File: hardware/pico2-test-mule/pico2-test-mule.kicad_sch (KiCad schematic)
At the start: 70 parts, among them J1 SPEAKER, J2 POWER, J3 AUX, J4 MOTOR, J5 VCC, Q1 DMN2991UDA-7B, Q10 DMN2991UDA-7B, Q11 DMN2991UDA-7B, Q12 DMN2991UDA-7B, Q13 DMN2991UDA-7B, Q2 SS8050, Q3 SS8050, Q4 DMN2991UDA-7B, Q5 SS8050, Q6 SS8050, Q7 NST847BPDP6T5G, Q8 SS8050, Q9 NST847BPDP6T5G, U1 NCS2220AMUT1G, U2 AP63203WU, U3 PICO, U4 MAX98357AEWL+T, U5 MD9927

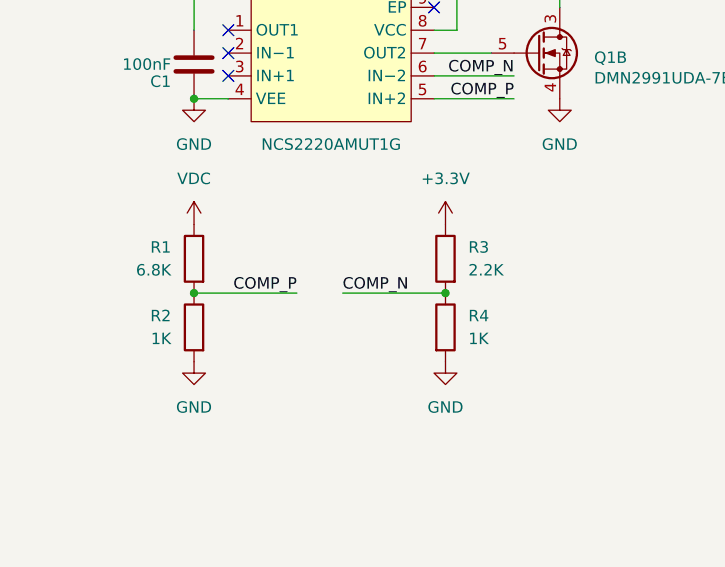
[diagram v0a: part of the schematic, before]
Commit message: fix: un-swap capacitor shutdown circuit inputs
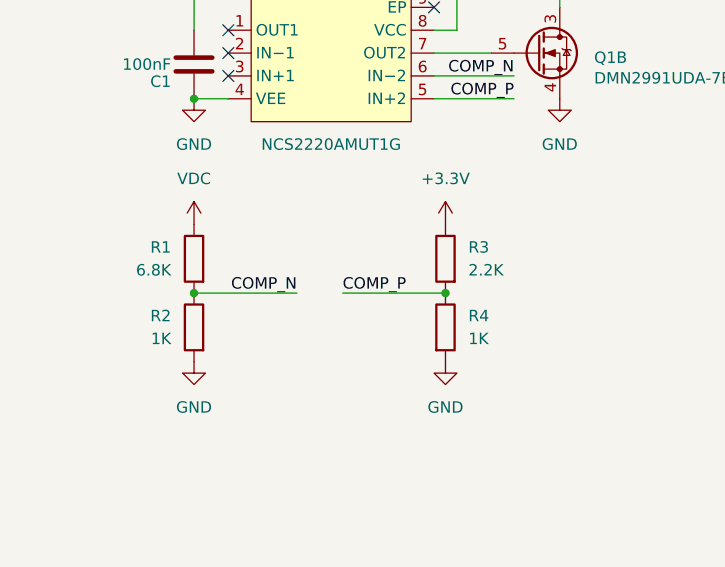
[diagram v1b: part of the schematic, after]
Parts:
- C1, C10, C3, C7, C9: footprint Capacitor_SMD:C_0402_1005Metric -> pico2-test-mule:C_0402_1005Metric
- C2, C4: footprint Capacitor_SMD:C_0603_1608Metric -> pico2-test-mule:C_0603_1608Metric
- C5, C8: footprint Capacitor_SMD:C_1206_3216Metric -> pico2-test-mule:C_1206_3216Metric
- C6: footprint Capacitor_SMD:C_0805_2012Metric -> pico2-test-mule:C_0805_2012Metric
- D10, D11, D12, D14, D15, D16, D17, D19, D3, D4, D5, D6, D9: footprint LED_SMD:LED_0603_1608Metric -> pico2-test-mule:LED_0603_1608Metric
- J1: footprint Connector_PinHeader_2.54mm:PinHeader_1x06_P2.54mm_Vertical -> pico2-test-mule:PinHeader_1x06_P2.54mm_Vertical
- J2: footprint Connector_PinHeader_2.54mm:PinHeader_1x04_P2.54mm_Vertical -> pico2-test-mule:PinHeader_1x04_P2.54mm_Vertical
- J3: footprint Connector_PinHeader_2.54mm:PinHeader_1x05_P2.54mm_Vertical -> pico2-test-mule:PinHeader_1x05_P2.54mm_Vertical
- J4, J5: footprint Connector_PinHeader_2.54mm:PinHeader_1x02_P2.54mm_Vertical -> pico2-test-mule:PinHeader_1x02_P2.54mm_Vertical
- Q2, Q3, Q5, Q6, Q8: footprint Package_TO_SOT_SMD:SOT-23 -> pico2-test-mule:SOT-23
- Q7, Q9: footprint Package_TO_SOT_SMD:SOT-963 -> pico2-test-mule:SOT-963
- R1, R10, R11, R12, R13, R14, R2, R3, R4, R5, R6, R7, R8, R9: footprint Resistor_SMD:R_0402_1005Metric -> pico2-test-mule:R_0402_1005Metric
- RN1, RN2, RN3: footprint Resistor_SMD:R_Array_Concave_4x0402 -> pico2-test-mule:R_Array_Concave_4x0402
- U3: footprint Module:RaspberryPi_Pico_Common_THT -> pico2-test-mule:RaspberryPi_Pico_Common_THT
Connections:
- net COMP_N: now also R1.2, R2.1; no longer R3.2, R4.1
- net COMP_P: now also R3.2, R4.1; no longer R1.2, R2.1
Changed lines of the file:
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@@
 	)
 	(label "COMP_N"
-		(at 58.42 157.48 0)
+		(at 53.34 157.48 180)
 		(effects
 			(font
 				(size 1.27 1.27)
 			)
-			(justify left bottom)
+			(justify right bottom)
 		)
 	)
 	(label "COMP_P"
-		(at 53.34 157.48 180)
+		(at 58.42 157.48 0)
 		(effects
 			(font
 				(size 1.27 1.27)
 			)
-			(justify right bottom)
+			(justify left bottom)
 		)
 	)
@@
 			)
 		)
-		(property "Footprint" "Resistor_SMD:R_0402_1005Metric"
+		(property "Footprint" "pico2-test-mule:R_0402_1005Metric"
 			(at 349.758 226.06 90)
 			(effects
@@
 			)
 		)
-		(property "Footprint" "Capacitor_SMD:C_1206_3216Metric"
+		(property "Footprint" "pico2-test-mule:C_1206_3216Metric"
 			(at 135.5852 55.88 0)
 			(effects
@@
 			)
 		)
-		(property "Footprint" "Package_TO_SOT_SMD:SOT-23"
+		(property "Footprint" "pico2-test-mule:SOT-23"
 			(at 107.95 241.046 0)
 			(effects
@@
 			)
 		)
-		(property "Footprint" "LED_SMD:LED_0603_1608Metric"
+		(property "Footprint" "pico2-test-mule:LED_0603_1608Metric"
 			(at 203.2 219.71 0)
 			(effects
@@
 			)
 		)
-		(property "Footprint" "Resistor_SMD:R_0402_1005Metric"
+		(property "Footprint" "pico2-test-mule:R_0402_1005Metric"
 			(at 68.072 161.29 90)
 			(effects
@@
 			)
 		)
-		(property "Footprint" "Capacitor_SMD:C_0402_1005Metric"
+		(property "Footprint" "pico2-test-mule:C_0402_1005Metric"
 			(at 38.989 129.7686 0)
 			(effects
@@
 			)
 		)
-		(property "Footprint" "Connector_PinHeader_2.54mm:PinHeader_1x02_P2.54mm_Vertical"
+		(property "Footprint" "pico2-test-mule:PinHeader_1x02_P2.54mm_Vertical"
 			(at 304.8 146.05 0)
 			(effects
@@
 			)
 		)
-		(property "Footprint" "Package_TO_SOT_SMD:SOT-963"
+		(property "Footprint" "pico2-test-mule:SOT-963"
 			(at 209.55 64.77 0)
 			(effects
@@
 			)
 		)
-		(property "Footprint" "Capacitor_SMD:C_0402_1005Metric"
+		(property "Footprint" "pico2-test-mule:C_0402_1005Metric"
 			(at 341.3252 148.59 0)
 			(effects
@@
 			)
 		)
-		(property "Footprint" "Resistor_SMD:R_Array_Concave_4x0402"
+		(property "Footprint" "pico2-test-mule:R_Array_Concave_4x0402"
 			(at 83.82 213.995 90)
 			(effects
@@
 			)
 		)
-		(property "Footprint" "Capacitor_SMD:C_0402_1005Metric"
+		(property "Footprint" "pico2-test-mule:C_0402_1005Metric"
 			(at 111.76 51.7652 0)
 			(effects
@@
 			)
 		)
-		(property "Footprint" "Connector_PinHeader_2.54mm:PinHeader_1x04_P2.54mm_Vertical"
+		(property "Footprint" "pico2-test-mule:PinHeader_1x04_P2.54mm_Vertical"
 			(at 243.84 252.73 0)
 			(effects
@@
 			)
 		)
-		(property "Footprint" "Package_TO_SOT_SMD:SOT-23"
+		(property "Footprint" "pico2-test-mule:SOT-23"
 			(at 214.63 234.696 0)
 			(effects
@@
 			)
 		)
-		(property "Footprint" "LED_SMD:LED_0603_1608Metric"
+		(property "Footprint" "pico2-test-mule:LED_0603_1608Metric"
 			(at 160.02 241.3 0)
 			(effects
@@
 			)
 		)
-		(property "Footprint" "Capacitor_SMD:C_0402_1005Metric"
+		(property "Footprint" "pico2-test-mule:C_0402_1005Metric"
 			(at 329.8952 148.59 0)
 			(effects
@@
 			)
 		)
-		(property "Footprint" "LED_SMD:LED_0603_1608Metric"
+		(property "Footprint" "pico2-test-mule:LED_0603_1608Metric"
 			(at 50.8 241.3 0)
 			(effects
@@
 			)
 		)
-		(property "Footprint" "LED_SMD:LED_0603_1608Metric"
+		(property "Footprint" "pico2-test-mule:LED_0603_1608Metric"
 			(at 50.8 252.73 0)
 			(effects
@@
 			)
 		)
-		(property "Footprint" "LED_SMD:LED_0603_1608Metric"
+		(property "Footprint" "pico2-test-mule:LED_0603_1608Metric"
 			(at 160.02 218.44 0)
 			(effects
@@
 			)
 		)
-		(property "Footprint" "Resistor_SMD:R_0402_1005Metric"
+		(property "Footprint" "pico2-test-mule:R_0402_1005Metric"
 			(at 210.312 49.53 90)
 			(effects
@@
 			)
 		)
-		(property "Footprint" "Package_TO_SOT_SMD:SOT-963"
+		(property "Footprint" "pico2-test-mule:SOT-963"
 			(at 226.06 55.88 0)
 			(effects
@@
 			)
 		)
-		(property "Footprint" "Resistor_SMD:R_Array_Concave_4x0402"
+		(property "Footprint" "pico2-test-mule:R_Array_Concave_4x0402"
 			(at 140.97 213.995 90)
 			(effects
@@
 			)
 		)
-		(property "Footprint" "Resistor_SMD:R_0402_1005Metric"
+		(property "Footprint" "pico2-test-mule:R_0402_1005Metric"
 			(at 371.602 226.06 90)
 			(effects
@@
 			)
 		)
-		(property "Footprint" "Resistor_SMD:R_0402_1005Metric"
+		(property "Footprint" "pico2-test-mule:R_0402_1005Metric"
 			(at 43.688 153.67 90)
 			(effects
@@
 			)
 		)
-		(property "Footprint" "Connector_PinHeader_2.54mm:PinHeader_1x06_P2.54mm_Vertical"
+		(property "Footprint" "pico2-test-mule:PinHeader_1x06_P2.54mm_Vertical"
 			(at 243.84 233.68 0)
 			(effects
@@
 			)
 		)
-		(property "Footprint" "Resistor_SMD:R_0402_1005Metric"
+		(property "Footprint" "pico2-test-mule:R_0402_1005Metric"
 			(at 371.602 236.22 90)
 			(effects
@@
 			)
 		)
-		(property "Footprint" "Resistor_SMD:R_0402_1005Metric"
+		(property "Footprint" "pico2-test-mule:R_0402_1005Metric"
 			(at 194.31 221.488 90)
 			(effects
@@
 			)
 		)
-		(property "Footprint" "Package_TO_SOT_SMD:SOT-963"
+		(property "Footprint" "pico2-test-mule:SOT-963"
 			(at 229.87 78.74 0)
 			(effects
@@
 			)
 		)
-		(property "Footprint" "Resistor_SMD:R_0402_1005Metric"
+		(property "Footprint" "pico2-test-mule:R_0402_1005Metric"
 			(at 153.162 52.07 90)
 			(effects
@@
 			)
 		)
-		(property "Footprint" "Resistor_SMD:R_Array_Concave_4x0402"
+		(property "Footprint" "pico2-test-mule:R_Array_Concave_4x0402"
 			(at 35.56 213.995 90)
 			(effects
@@
 			)
 		)
-		(property "Footprint" "LED_SMD:LED_0603_1608Metric"
+		(property "Footprint" "pico2-test-mule:LED_0603_1608Metric"
 			(at 160.02 229.87 0)
 			(effects
@@
 			)
 		)
-		(property "Footprint" "Resistor_SMD:R_0402_1005Metric"
+		(property "Footprint" "pico2-test-mule:R_0402_1005Metric"
 			(at 349.758 236.22 90)
 			(effects
@@
 			)
 		)
-		(property "Footprint" "Resistor_SMD:R_0402_1005Metric"
+		(property "Footprint" "pico2-test-mule:R_0402_1005Metric"
 			(at 43.688 161.29 90)
 			(effects
@@
 			)
 		)
-		(property "Footprint" "Resistor_SMD:R_0402_1005Metric"
+		(property "Footprint" "pico2-test-mule:R_0402_1005Metric"
 			(at 215.9 83.058 90)
 			(effects
@@
 			)
 		)
-		(property "Footprint" "Capacitor_SMD:C_0603_1608Metric"
+		(property "Footprint" "pico2-test-mule:C_0603_1608Metric"
 			(at 79.0448 63.5 0)
 			(effects
@@
 			)
 		)
-		(property "Footprint" "LED_SMD:LED_0603_1608Metric"
+		(property "Footprint" "pico2-test-mule:LED_0603_1608Metric"
 			(at 99.06 256.54 0)
 			(effects
@@
 			)
 		)
-		(property "Footprint" "Capacitor_SMD:C_0402_1005Metric"
+		(property "Footprint" "pico2-test-mule:C_0402_1005Metric"
 			(at 381.3048 210.82 0)
 			(effects
@@
 			)
 		)
-		(property "Footprint" "Resistor_SMD:R_0402_1005Metric"
+		(property "Footprint" "pico2-test-mule:R_0402_1005Metric"
 			(at 71.628 153.67 90)
 			(effects
@@
 			)
 		)
-		(property "Footprint" "Capacitor_SMD:C_0805_2012Metric"
+		(property "Footprint" "pico2-test-mule:C_0805_2012Metric"
 			(at 148.2852 67.31 0)
 			(effects
@@
 			)
 		)
-		(property "Footprint" "Capacitor_SMD:C_1206_3216Metric"
+		(property "Footprint" "pico2-test-mule:C_1206_3216Metric"
 			(at 331.7748 210.82 0)
 			(effects
@@
 			)
 		)
-		(property "Footprint" "Package_TO_SOT_SMD:SOT-23"
+		(property "Footprint" "pico2-test-mule:SOT-23"
 			(at 167.64 272.796 0)
 			(effects
@@
 			)
 		)
-		(property "Footprint" "Module:RaspberryPi_Pico_Common_THT"
+		(property "Footprint" "pico2-test-mule:RaspberryPi_Pico_Common_THT"
 			(at 255.27 196.85 0)
 			(effects
@@
 			)
 		)
-		(property "Footprint" "Resistor_SMD:R_0402_1005Metric"
+		(property "Footprint" "pico2-test-mule:R_0402_1005Metric"
 			(at 229.87 60.452 90)
 			(effects
@@
 			)
 		)
-		(property "Footprint" "Package_TO_SOT_SMD:SOT-963"
+		(property "Footprint" "pico2-test-mule:SOT-963"
 			(at 201.93 78.74 0)
 			(effects
@@
 			)
 		)
-		(property "Footprint" "Capacitor_SMD:C_0603_1608Metric"
+		(property "Footprint" "pico2-test-mule:C_0603_1608Metric"
 			(at 124.1552 55.88 0)
 			(effects
@@
 			)
 		)
-		(property "Footprint" "LED_SMD:LED_0603_1608Metric"
+		(property "Footprint" "pico2-test-mule:LED_0603_1608Metric"
 			(at 99.06 212.09 0)
 			(effects
@@
 			)
 		)
-		(property "Footprint" "LED_SMD:LED_0603_1608Metric"
+		(property "Footprint" "pico2-test-mule:LED_0603_1608Metric"
 			(at 99.06 228.6 0)
 			(effects
@@
 			)
 		)
-		(property "Footprint" "LED_SMD:LED_0603_1608Metric"
+		(property "Footprint" "pico2-test-mule:LED_0603_1608Metric"
 			(at 50.8 218.44 0)
 			(effects
@@
 			)
 		)
-		(property "Footprint" "LED_SMD:LED_0603_1608Metric"
+		(property "Footprint" "pico2-test-mule:LED_0603_1608Metric"
 			(at 50.8 229.87 0)
 			(effects
@@
 			)
 		)
-		(property "Footprint" "Package_TO_SOT_SMD:SOT-23"
+		(property "Footprint" "pico2-test-mule:SOT-23"
 			(at 107.95 224.536 0)
 			(effects
@@
 			)
 		)
-		(property "Footprint" "Package_TO_SOT_SMD:SOT-23"
+		(property "Footprint" "pico2-test-mule:SOT-23"
 			(at 167.64 253.746 0)
 			(effects
@@
 			)
 		)
-		(property "Footprint" "LED_SMD:LED_0603_1608Metric"
+		(property "Footprint" "pico2-test-mule:LED_0603_1608Metric"
 			(at 99.06 245.11 0)
 			(effects
@@
 			)
 		)
-		(property "Footprint" "Resistor_SMD:R_0402_1005Metric"
+		(property "Footprint" "pico2-test-mule:R_0402_1005Metric"
 			(at 153.162 63.5 90)
 			(effects
@@
 			)
 		)
-		(property "Footprint" "Connector_PinHeader_2.54mm:PinHeader_1x05_P2.54mm_Vertical"
+		(property "Footprint" "pico2-test-mule:PinHeader_1x05_P2.54mm_Vertical"
 			(at 274.32 240.03 0)
 			(effects
@@
 			)
 		)
-		(property "Footprint" "LED_SMD:LED_0603_1608Metric"
+		(property "Footprint" "pico2-test-mule:LED_0603_1608Metric"
 			(at 160.02 260.35 0)
 			(effects
@@
 			)
 		)
-		(property "Footprint" "Connector_PinHeader_2.54mm:PinHeader_1x02_P2.54mm_Vertical"
+		(property "Footprint" "pico2-test-mule:PinHeader_1x02_P2.54mm_Vertical"
 			(at 274.32 254 0)
 			(effects
